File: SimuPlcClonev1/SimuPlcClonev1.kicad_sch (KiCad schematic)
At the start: 1 part

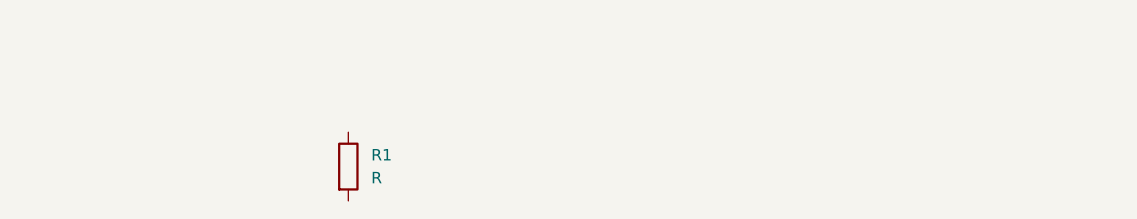
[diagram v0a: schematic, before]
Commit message: Agregado Resistencias
solo agreg 2 nuevas resistencias para verificar cambios.
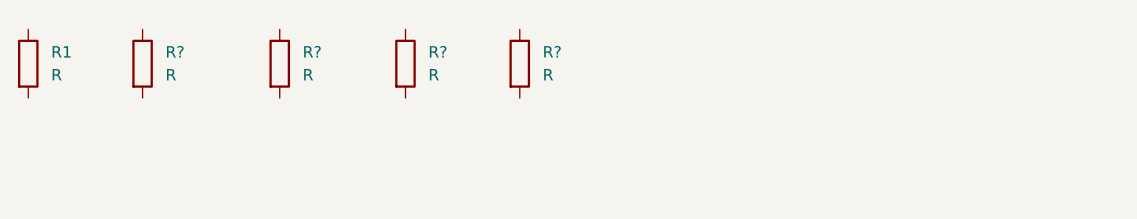
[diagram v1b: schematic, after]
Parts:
- added R? (x4): R, symbol Device:R
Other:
- moved on the sheet: R1

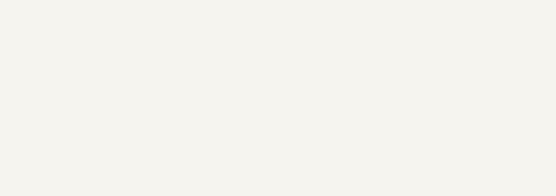
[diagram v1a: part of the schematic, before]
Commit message: nuevas resistencia agregadas
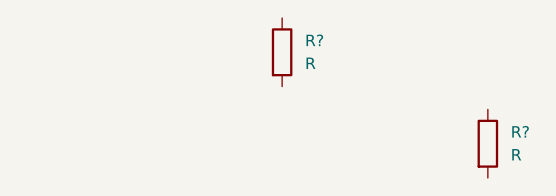
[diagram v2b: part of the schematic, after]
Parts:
- added R? (x2): R, symbol Device:R
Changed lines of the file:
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@@
+	(symbol
+		(lib_id "Device:R")
+		(at 175.26 43.18 0)
+		(unit 1)
+		(exclude_from_sim no)
+		(in_bom yes)
+		(on_board yes)
+		(dnp no)
+		(fields_autoplaced yes)
+		(property "Reference" "R?"
+			(at 177.8 41.9099 0)
+			(effects
+				(font
+					(size 1.27 1.27)
+				)
+				(justify left)
+			)
+		)
+		(property "Value" "R"
+			(at 177.8 44.4499 0)
+			(effects
+				(font
+					(size 1.27 1.27)
+				)
+				(justify left)
+			)
+		)
+		(property "Footprint" ""
+			(at 173.482 43.18 90)
+			(effects
+				(font
+					(size 1.27 1.27)
+				)
+				(hide yes)
+			)
+		)
+		(property "Datasheet" "~"
+			(at 175.26 43.18 0)
+			(effects
+				(font
+					(size 1.27 1.27)
+				)
+				(hide yes)
+			)
+		)
+		(property "Description" "Resistor"
+			(at 175.26 43.18 0)
+			(effects
+				(font
+					(size 1.27 1.27)
+				)
+				(hide yes)
+			)
+		)
+		(pin "2"
+		)
+		(pin "1"
+		)
+		(instances
+			(project "SimuPlcClonev1"
+				(path "/9554bc7d-464a-41dc-8945-3da7c192c12a"
+					(reference "R?")
+					(unit 1)
+				)
+			)
+		)
+	)
 	(symbol
 		(lib_id "Device:R")
@@
 			(effects
 				(font
+					(size 1.27 1.27)
+				)
+				(hide yes)
+			)
+		)
+		(pin "2"
+		)
+		(pin "1"
+		)
+		(instances
+			(project "SimuPlcClonev1"
+				(path "/9554bc7d-464a-41dc-8945-3da7c192c12a"
+					(reference "R?")
+					(unit 1)
+				)
+			)
+		)
+	)
+	(symbol
+		(lib_id "Device:R")
+		(at 198.12 53.34 0)
+		(unit 1)
+		(exclude_from_sim no)
+		(in_bom yes)
+		(on_board yes)
+		(dnp no)
+		(fields_autoplaced yes)
+		(property "Reference" "R?"
+			(at 200.66 52.0699 0)
+			(effects
+				(font
+					(size 1.27 1.27)
+				)
+				(justify left)
+			)
+		)
+		(property "Value" "R"
+			(at 200.66 54.6099 0)
+			(effects
+				(font
+					(size 1.27 1.27)
+				)
+				(justify left)
+			)
+		)
+		(property "Footprint" ""
+			(at 196.342 53.34 90)
+			(effects
+				(font
+					(size 1.27 1.27)
+				)
+				(hide yes)
+			)
+		)
+		(property "Datasheet" "~"
+			(at 198.12 53.34 0)
+			(effects
+				(font
+					(size 1.27 1.27)
+				)
+				(hide yes)
+			)
+		)
+		(property "Description" "Resistor"
+			(at 198.12 53.34 0)
+			(effects
+				(font
